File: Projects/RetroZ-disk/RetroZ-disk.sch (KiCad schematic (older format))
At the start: 22 parts, among them J1 Micro_SD_Card, J2 IO SELECTOR, Q1 2SA933, U1 UA78M33CDCYR, U2 74LS138, U3 TXB0104DW, U4 ATMEGA328P-PU, U5 74LS02, Y1 20Mhz

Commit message: added interrupt signal
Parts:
- added Q2: 2SA933, Package_TO_SOT_THT:TO-92S_Wide, symbol Device:Q_PNP_ECB
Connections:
- net GND: now also Q2.2 (C)
- net ~INT: now reaches I1.30 (~INT~)
- net ~INT: now also Q2.1 (E)
- net at U4.14 ((PCINT0/CLKO/ICP1)PB0): now also Q2.3 (B)
- no-connect marks 39 -> 37
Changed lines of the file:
@@
 NoConn ~ 1175 1400
 NoConn ~ 1175 1700
-NoConn ~ 1175 1800
 NoConn ~ 1175 2200
 NoConn ~ 1175 2400
@@
 Text Label 9900 5175 2    50   ~ 0
 ~WAIT
-NoConn ~ 7800 1550
 Text Label 8100 2800 2    50   ~ 0
 ~CS
@@
 	0    1    1    0
 $EndComp
+$Comp
+L Device:Q_PNP_ECB Q2
+U 1 1 5E6AC7AF
+P 8475 1200
+F 0 "Q2" H 8400 1075 50  0000 C CNN
+F 1 "2SA933" H 8800 1225 50  0000 C CNN
+F 2 "Package_TO_SOT_THT:TO-92S_Wide" H 8675 1300 50  0001 C CNN
+F 3 "https://media.digikey.com/pdf/Data%20Sheets/Micro%20Commercial%20PDFs/2SA933AS-x.pdf" H 8475 1200 50  0001 C CNN
+	1    8475 1200
+	1    0    0    1
+$EndComp
+$Comp
+L power:GND #PWR0101
+U 1 1 5E6C653E
+P 8575 1400
+F 0 "#PWR0101" H 8575 1150 50  0001 C CNN
+F 1 "GND" H 8575 1250 50  0000 C CNN
+F 2 "" H 8575 1400 50  0001 C CNN
+F 3 "" H 8575 1400 50  0001 C CNN
+	1    8575 1400
+	1    0    0    -1
+$EndComp
+Text Label 8750 1000 2    50   ~ 0
+~INT
+Wire Wire Line
+	8575 1000 8750 1000
+Wire Wire Line
+	7800 1550 7800 1200
+Wire Wire Line
+	7800 1200 8275 1200
+Text Label 925  1800 0    50   ~ 0
+~INT
+Wire Wire Line
+	1175 1800 925  1800
 Wire Bus Line
 	8075 3250 8075 4300

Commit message: fixed interrupt ack processing
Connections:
- net ~IORQ: now also U4.14 ((PCINT0/CLKO/ICP1)PB0)
- net ~M1: now reaches I1.31 (~M1~)
- net ~M1: now also U4.15 ((PCINT1/OC1A)PB1)
- net at Q2.3 (B): now also U4.28 ((PCINT13/SCL/ADC5)PC5); no longer U4.14 ((PCINT0/CLKO/ICP1)PB0)
- no-connect marks 37 -> 33
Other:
- moved on the sheet: Q2
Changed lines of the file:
@@
 Wire Wire Line
 	5400 5700 5400 5600
-NoConn ~ 1175 2100
 Text Notes 1900 5050 0    50   ~ 0
 5V to 3.3V,500mA
@@
 	0    -1   -1   0
 $EndComp
-NoConn ~ 5950 2575
 $Comp
 L power:VDD #PWR013
@@
 	1    0    0    -1
 $EndComp
-NoConn ~ 7800 1650
 Wire Wire Line
 	8700 1750 8925 1750
@@
 Wire Wire Line
 	9150 2800 9175 2800
-NoConn ~ 7800 2900
 $Comp
 L power:GND #PWR020
@@
 L Device:Q_PNP_ECB Q2
 U 1 1 5E6AC7AF
-P 8475 1200
-F 0 "Q2" H 8400 1075 50  0000 C CNN
-F 1 "2SA933" H 8800 1225 50  0000 C CNN
-F 2 "Package_TO_SOT_THT:TO-92S_Wide" H 8675 1300 50  0001 C CNN
-F 3 "https://media.digikey.com/pdf/Data%20Sheets/Micro%20Commercial%20PDFs/2SA933AS-x.pdf" H 8475 1200 50  0001 C CNN
-	1    8475 1200
+P 9025 2250
+F 0 "Q2" H 8950 2125 50  0000 C CNN
+F 1 "2SA933" H 9350 2275 50  0000 C CNN
+F 2 "Package_TO_SOT_THT:TO-92S_Wide" H 9225 2350 50  0001 C CNN
+F 3 "https://media.digikey.com/pdf/Data%20Sheets/Micro%20Commercial%20PDFs/2SA933AS-x.pdf" H 9025 2250 50  0001 C CNN
+	1    9025 2250
 	1    0    0    1
 $EndComp
@@
 L power:GND #PWR0101
 U 1 1 5E6C653E
-P 8575 1400
-F 0 "#PWR0101" H 8575 1150 50  0001 C CNN
-F 1 "GND" H 8575 1250 50  0000 C CNN
-F 2 "" H 8575 1400 50  0001 C CNN
-F 3 "" H 8575 1400 50  0001 C CNN
-	1    8575 1400
-	1    0    0    -1
-$EndComp
-Text Label 8750 1000 2    50   ~ 0
+P 9125 2450
+F 0 "#PWR0101" H 9125 2200 50  0001 C CNN
+F 1 "GND" H 9125 2300 50  0000 C CNN
+F 2 "" H 9125 2450 50  0001 C CNN
+F 3 "" H 9125 2450 50  0001 C CNN
+	1    9125 2450
+	1    0    0    -1
+$EndComp
+Text Label 9300 2050 2    50   ~ 0
 ~INT
 Wire Wire Line
-	8575 1000 8750 1000
-Wire Wire Line
-	7800 1550 7800 1200
-Wire Wire Line
-	7800 1200 8275 1200
+	9125 2050 9300 2050
 Text Label 925  1800 0    50   ~ 0
 ~INT
 Wire Wire Line
 	1175 1800 925  1800
+Wire Wire Line
+	1175 2100 925  2100
+Text Label 925  2100 0    50   ~ 0
+~M1
+Wire Wire Line
+	7800 1650 8100 1650
+Text Label 8100 1650 2    50   ~ 0
+~M1
+Text Label 8100 1550 2    50   ~ 0
+~IORQ
+Wire Wire Line
+	7800 1550 8100 1550
+Wire Wire Line
+	8825 2250 8800 2250
+Wire Wire Line
+	8800 2250 8800 2900
+Wire Wire Line
+	8800 2900 7800 2900
 Wire Bus Line
 	8075 3250 8075 4300

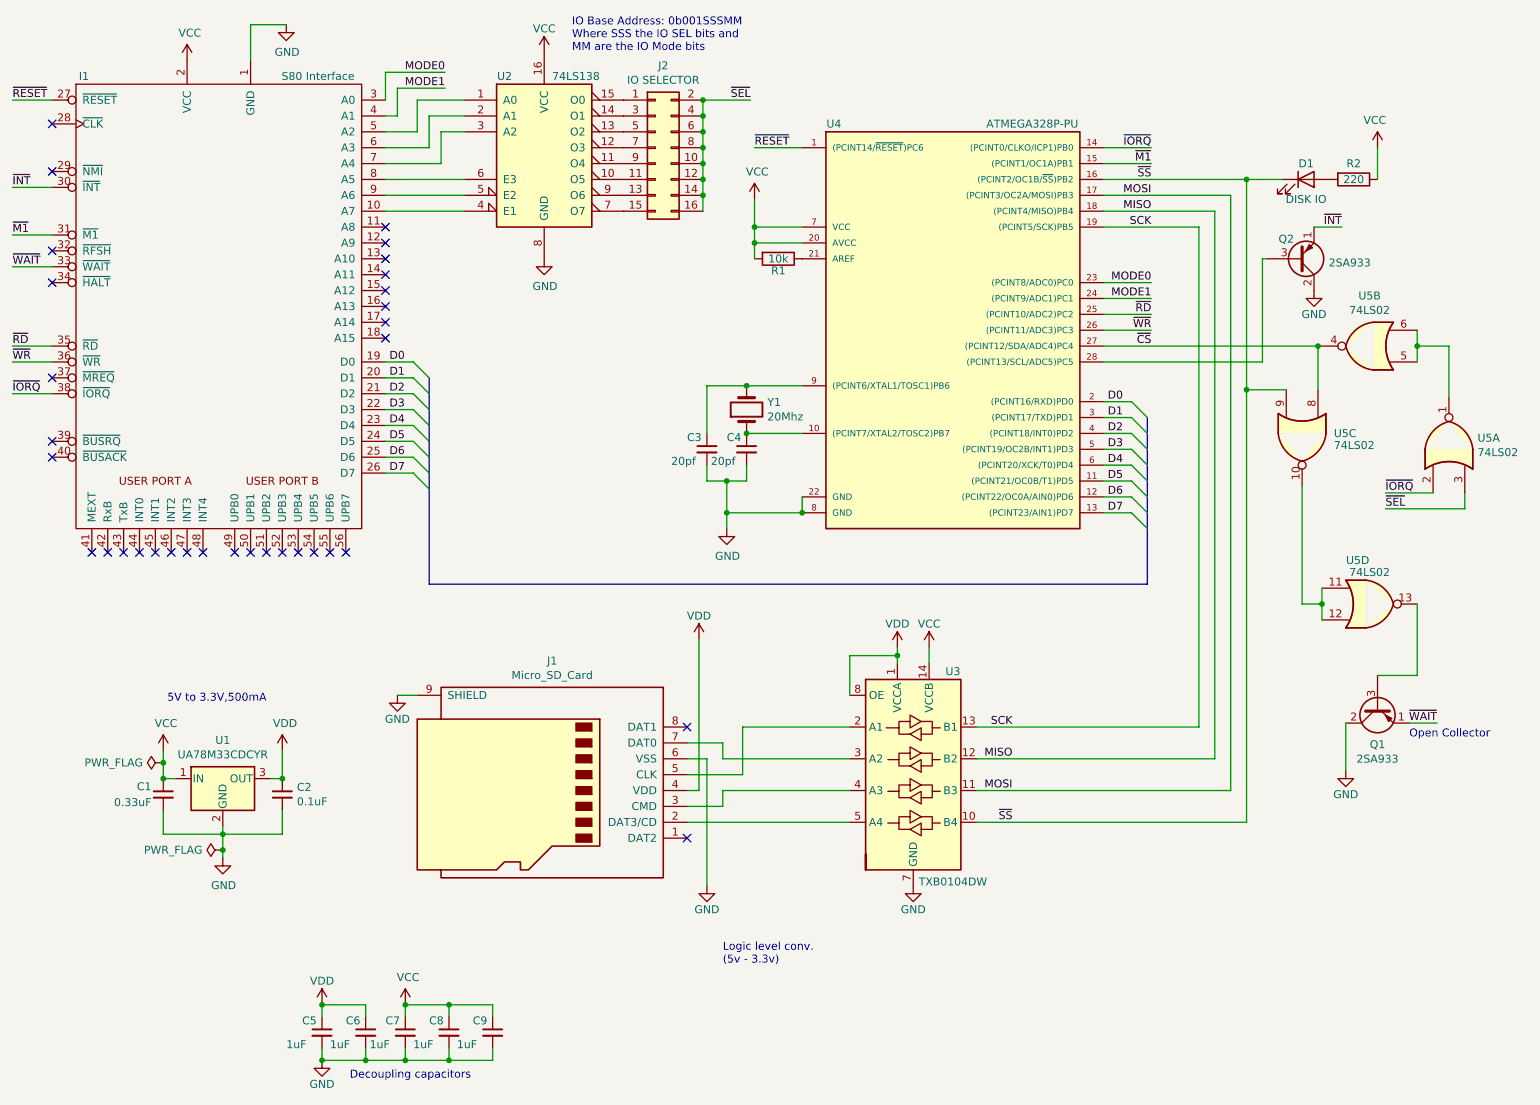
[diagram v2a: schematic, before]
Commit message: removed interrupt management, added arduino code
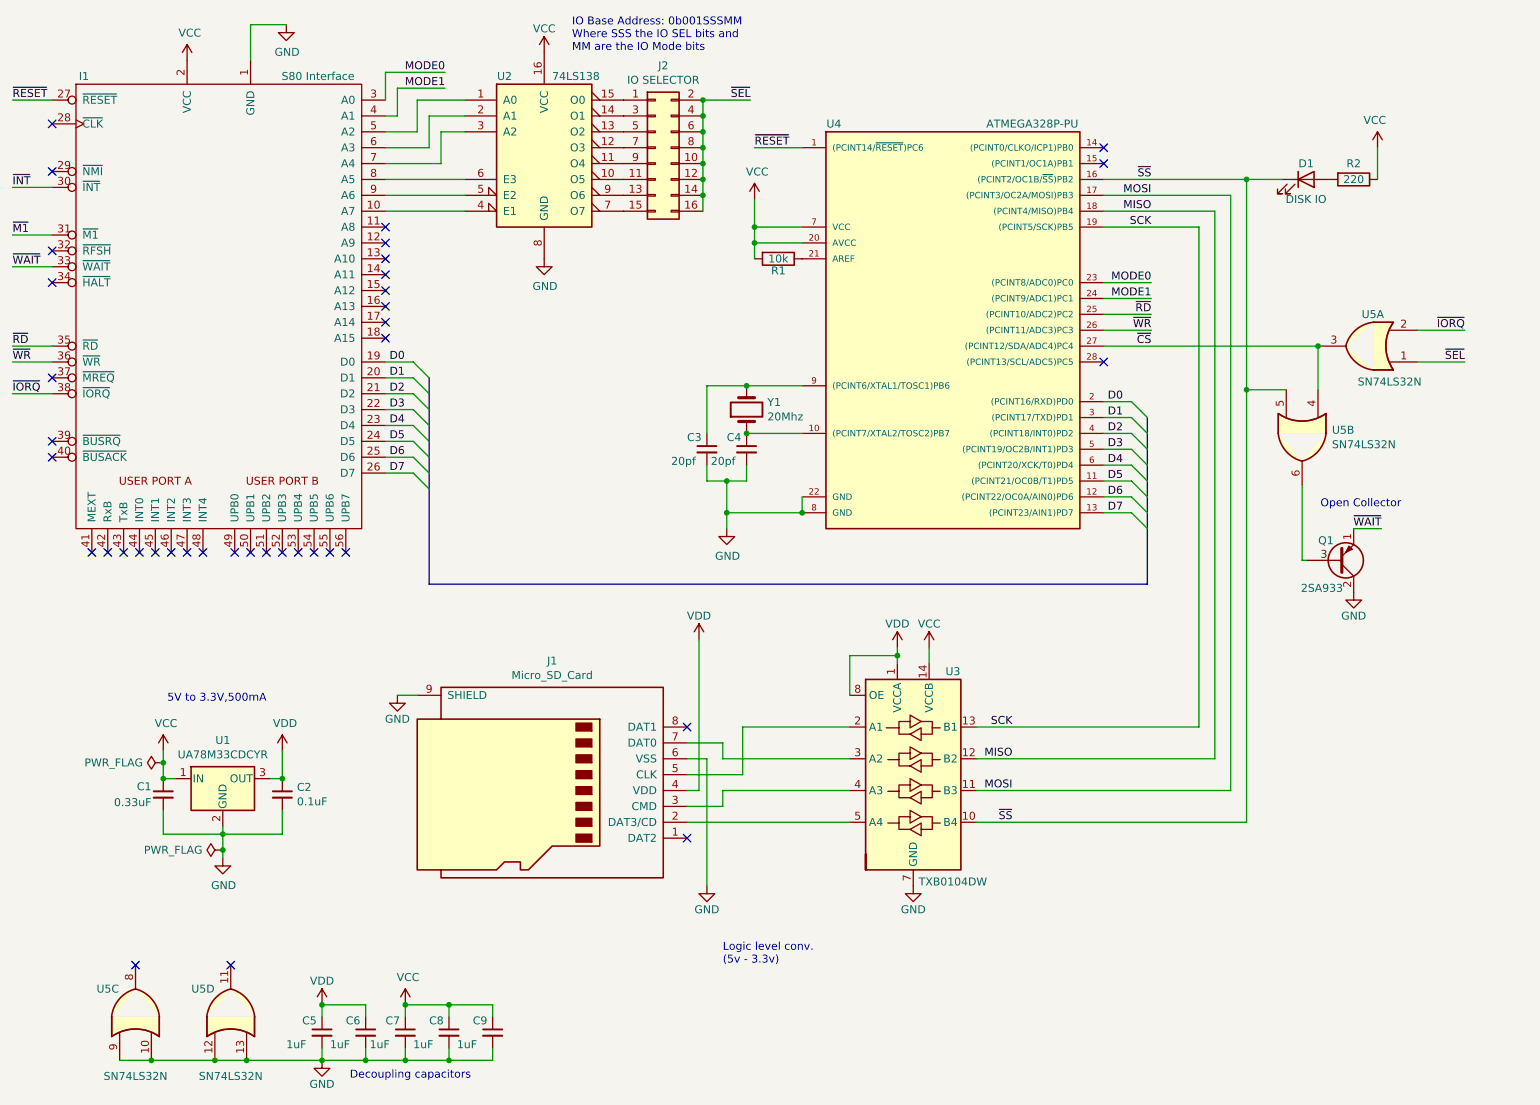
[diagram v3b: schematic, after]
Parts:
- removed Q2: 2SA933, Package_TO_SOT_THT:TO-92S_Wide, symbol Device:Q_PNP_ECB
- removed U5: 74LS02, symbol 74xx:7402
- added U5: SN74LS32N, Package_DIP:DIP-14_W7.62mm_LongPads, symbol 74xx:74LS32
- U2: footprint Housings_DIP:DIP-16_W7.62mm_Socket_LongPads -> Package_DIP:DIP-16_W7.62mm_LongPads
- U4: footprint Housings_DIP:DIP-28_W7.62mm_Socket_LongPads -> Package_DIP:DIP-28_W7.62mm_LongPads
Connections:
- net GND: now also U5.10, U5.12, U5.13, U5.9
- net ~CS: now also U5.3, U5.4
- net ~IORQ: now also U5.2; no longer U4.14 ((PCINT0/CLKO/ICP1)PB0)
- net ~M1: no longer U4.15 ((PCINT1/OC1A)PB1)
- net ~SEL: now also U5.1
- net ~SS: now also U5.5
- net at Q1.3 (B): now also U5.6
- no-connect marks 33 -> 38
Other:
- moved on the sheet: Q1
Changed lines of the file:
@@
 F 0 "U4" H 6100 3900 50  0000 C CNN
 F 1 "ATMEGA328P-PU" H 7350 3900 50  0000 C CNN
-F 2 "Housings_DIP:DIP-28_W7.62mm_Socket_LongPads" H 6800 2650 50  0001 C CIN
+F 2 "Package_DIP:DIP-28_W7.62mm_LongPads" H 6800 2650 50  0001 C CIN
 F 3 "https://www.mouser.ca/datasheet/2/268/Atmel-8271-8-bit-AVR-Microcontroller-ATmega48A-48P-1315288.pdf" H 6800 2650 50  0001 C CNN
 	1    6800 2650
@@
 F 0 "U2" H 4025 2000 50  0000 C CNN
 F 1 "74LS138" H 4475 2000 50  0000 C CNN
-F 2 "Housings_DIP:DIP-16_W7.62mm_Socket_LongPads" H 4275 1550 50  0001 C CNN
+F 2 "Package_DIP:DIP-16_W7.62mm_LongPads" H 4275 1550 50  0001 C CNN
 F 3 "http://www.ti.com/lit/gpn/sn74LS138" H 4275 1550 50  0001 C CNN
 F 4 "SN74HC138N" H 4275 1550 50  0001 C CNN "Mfr#"
@@
 Text Label 925  3100 0    50   ~ 0
 ~IORQ
-Text Label 9575 3725 0    50   ~ 0
+Text Label 10075 2700 2    50   ~ 0
 ~IORQ
 Wire Wire Line
-	9875 3725 9575 3725
+	9775 2700 10075 2700
 Text Label 5575 1250 2    50   ~ 0
 ~SEL
@@
 	5275 1250 5575 1250
 Connection ~ 5275 1250
-Text Label 9575 3825 0    50   ~ 0
+Text Label 10075 2900 2    50   ~ 0
 ~SEL
 Wire Bus Line
@@
 	2250 5875 2250 5975
 Connection ~ 2250 5975
-Text Label 9900 5175 2    50   ~ 0
+Text Label 9550 3950 2    50   ~ 0
 ~WAIT
 Text Label 8100 2800 2    50   ~ 0
 ~CS
-$Comp
-L 74xx:7402 U5
-U 2 1 5E2FF702
-P 9475 2800
-F 0 "U5" H 9475 2483 50  0000 C CNN
-F 1 "74LS02" H 9475 2574 50  0000 C CNN
-F 2 "" H 9475 2800 50  0001 C CNN
-F 3 "http://www.ti.com/lit/gpn/sn74ls02" H 9475 2800 50  0001 C CNN
-	2    9475 2800
-	-1   0    0    1
-$EndComp
-Wire Wire Line
-	9775 2700 9775 2800
-Wire Wire Line
-	9975 3125 9975 2800
-Wire Wire Line
-	9975 2800 9775 2800
-Connection ~ 9775 2800
-Wire Wire Line
-	9775 2800 9775 2900
-Wire Wire Line
-	10075 3825 10075 3725
-Wire Wire Line
-	9575 3825 10075 3825
 Wire Wire Line
 	3275 1750 3775 1750
 Text Notes 4450 950  0    50   ~ 0
 IO Base Address: 0b001SSSMM\nWhere SSS the IO SEL bits and\nMM are the IO Mode bits
-$Comp
-L 74xx:7402 U5
-U 1 1 5E34E3AC
-P 9975 3425
-F 0 "U5" V 10021 3245 50  0000 R CNN
-F 1 "74LS02" V 9930 3245 50  0000 R CNN
-F 2 "Housings_DIP:DIP-14_W7.62mm_Socket_LongPads" H 9975 3425 50  0001 C CNN
-F 3 "http://www.ti.com/lit/gpn/sn74ls02" H 9975 3425 50  0001 C CNN
-F 4 "SN74HC02NE4" V 9975 3425 50  0001 C CNN "Mfr#"
-	1    9975 3425
-	0    -1   -1   0
-$EndComp
 $Comp
 L power:VDD #PWR013
@@
 L power:GND #PWR020
 U 1 1 5E7A07A4
-P 9325 5475
-F 0 "#PWR020" H 9325 5225 50  0001 C CNN
-F 1 "GND" H 9325 5325 50  0000 C CNN
-F 2 "" H 9325 5475 50  0001 C CNN
-F 3 "" H 9325 5475 50  0001 C CNN
-	1    9325 5475
-	1    0    0    -1
-$EndComp
-Text Notes 9725 5275 0    50   ~ 0
+P 9375 4350
+F 0 "#PWR020" H 9375 4100 50  0001 C CNN
+F 1 "GND" H 9375 4200 50  0000 C CNN
+F 2 "" H 9375 4350 50  0001 C CNN
+F 3 "" H 9375 4350 50  0001 C CNN
+	1    9375 4350
+	1    0    0    -1
+$EndComp
+Text Notes 9675 3825 2    50   ~ 0
 Open Collector
 Wire Wire Line
-	9725 5175 9900 5175
+	9375 3950 9550 3950
 $Comp
 L Device:Q_PNP_ECB Q1
 U 1 1 5E7F9FF3
-P 9525 5075
-F 0 "Q1" V 9760 5075 50  0000 C CNN
-F 1 "2SA933" V 9851 5075 50  0000 C CNN
-F 2 "Package_TO_SOT_THT:TO-92S_Wide" H 9725 5175 50  0001 C CNN
-F 3 "https://media.digikey.com/pdf/Data%20Sheets/Micro%20Commercial%20PDFs/2SA933AS-x.pdf" H 9525 5075 50  0001 C CNN
-	1    9525 5075
-	0    -1   1    0
-$EndComp
-Wire Wire Line
-	9325 5175 9325 5475
-Wire Wire Line
-	9175 4325 9175 4425
-Wire Wire Line
-	9050 3675 9050 4425
-Wire Wire Line
-	9050 4425 9175 4425
-Connection ~ 9175 4425
-Wire Wire Line
-	9175 4425 9175 4525
-Wire Wire Line
-	9775 4425 9775 4875
-Wire Wire Line
-	9775 4875 9525 4875
-$Comp
-L 74xx:7402 U5
-U 4 1 5E88BC6D
-P 9475 4425
-F 0 "U5" H 9400 4700 50  0000 C CNN
-F 1 "74LS02" H 9475 4625 50  0000 C CNN
-F 2 "" H 9475 4425 50  0001 C CNN
-F 3 "http://www.ti.com/lit/gpn/sn74ls02" H 9475 4425 50  0001 C CNN
-	4    9475 4425
-	1    0    0    -1
-$EndComp
-$Comp
-L 74xx:7402 U5
-U 3 1 5E8A09DC
-P 9050 3375
-F 0 "U5" V 9025 3575 50  0000 L CNN
-F 1 "74LS02" V 9100 3575 50  0000 L CNN
-F 2 "" H 9050 3375 50  0001 C CNN
-F 3 "http://www.ti.com/lit/gpn/sn74ls02" H 9050 3375 50  0001 C CNN
-F 4 "SN74HC02NE4" V 9050 3375 50  0001 C CNN "Mfr#"
-	3    9050 3375
-	0    1    1    0
-$EndComp
-$Comp
-L Device:Q_PNP_ECB Q2
-U 1 1 5E6AC7AF
-P 9025 2250
-F 0 "Q2" H 8950 2125 50  0000 C CNN
-F 1 "2SA933" H 9350 2275 50  0000 C CNN
-F 2 "Package_TO_SOT_THT:TO-92S_Wide" H 9225 2350 50  0001 C CNN
-F 3 "https://media.digikey.com/pdf/Data%20Sheets/Micro%20Commercial%20PDFs/2SA933AS-x.pdf" H 9025 2250 50  0001 C CNN
-	1    9025 2250
+P 9275 4150
+F 0 "Q1" H 9200 4025 50  0000 C CNN
+F 1 "2SA933" H 9175 4325 50  0000 C CNN
+F 2 "Package_TO_SOT_THT:TO-92S_Wide" H 9475 4250 50  0001 C CNN
+F 3 "https://media.digikey.com/pdf/Data%20Sheets/Micro%20Commercial%20PDFs/2SA933AS-x.pdf" H 9275 4150 50  0001 C CNN
+	1    9275 4150
 	1    0    0    1
 $EndComp
-$Comp
-L power:GND #PWR0101
-U 1 1 5E6C653E
-P 9125 2450
-F 0 "#PWR0101" H 9125 2200 50  0001 C CNN
-F 1 "GND" H 9125 2300 50  0000 C CNN
-F 2 "" H 9125 2450 50  0001 C CNN
-F 3 "" H 9125 2450 50  0001 C CNN
-	1    9125 2450
-	1    0    0    -1
-$EndComp
-Text Label 9300 2050 2    50   ~ 0
-~INT
-Wire Wire Line
-	9125 2050 9300 2050
 Text Label 925  1800 0    50   ~ 0
 ~INT
@@
 Text Label 925  2100 0    50   ~ 0
 ~M1
-Wire Wire Line
-	7800 1650 8100 1650
-Text Label 8100 1650 2    50   ~ 0
-~M1
-Text Label 8100 1550 2    50   ~ 0
-~IORQ
-Wire Wire Line
-	7800 1550 8100 1550
-Wire Wire Line
-	8825 2250 8800 2250
-Wire Wire Line
-	8800 2250 8800 2900
-Wire Wire Line
-	8800 2900 7800 2900
+$Comp
+L 74xx:74LS32 U5
+U 1 1 5E7FD5C4
+P 9475 2800
+F 0 "U5" H 9525 2600 50  0000 R CNN
+F 1 "SN74LS32N" H 9550 3025 50  0000 R CNN
+F 2 "Package_DIP:DIP-14_W7.62mm_LongPads" H 9475 2800 50  0001 C CNN
+F 3 "http://www.ti.com/lit/gpn/sn74LS32" H 9475 2800 50  0001 C CNN
+	1    9475 2800
+	-1   0    0    1
+$EndComp
+Wire Wire Line
+	9775 2900 10075 2900
+$Comp
+L 74xx:74LS32 U5
+U 2 1 5E83A9D0
+P 9050 3375
+F 0 "U5" V 9004 3563 50  0000 L CNN
+F 1 "SN74LS32N" V 9095 3563 50  0000 L CNN
+F 2 "Package_DIP:DIP-14_W7.62mm_LongPads" H 9050 3375 50  0001 C CNN
+F 3 "http://www.ti.com/lit/gpn/sn74LS32" H 9050 3375 50  0001 C CNN
+	2    9050 3375
+	0    1    1    0
+$EndComp
+Wire Wire Line
+	9050 3675 9050 4150
+Wire Wire Line
+	9050 4150 9075 4150
+$Comp
+L 74xx:74LS32 U5
+U 3 1 5E886F65
+P 1700 7000
+F 0 "U5" V 1850 7175 50  0000 C CNN
+F 1 "SN74LS32N" V 1300 7000 50  0000 C CNN
+F 2 "Package_DIP:DIP-14_W7.62mm_LongPads" H 1700 7000 50  0001 C CNN
+F 3 "http://www.ti.com/lit/gpn/sn74LS32" H 1700 7000 50  0001 C CNN
+	3    1700 7000
+	0    -1   -1   0
+$EndComp
+$Comp
+L 74xx:74LS32 U5
+U 4 1 5E8895AC
+P 2300 7000
+F 0 "U5" V 2450 7175 50  0000 C CNN
+F 1 "SN74LS32N" V 1900 7000 50  0000 C CNN
+F 2 "Package_DIP:DIP-14_W7.62mm_LongPads" H 2300 7000 50  0001 C CNN
+F 3 "http://www.ti.com/lit/gpn/sn74LS32" H 2300 7000 50  0001 C CNN
+	4    2300 7000
+	0    -1   -1   0
+$EndComp
+NoConn ~ 1700 6700
+NoConn ~ 2300 6700
+Wire Wire Line
+	2875 7300 2400 7300
+Connection ~ 1800 7300
+Wire Wire Line
+	1800 7300 1600 7300
+Connection ~ 2200 7300
+Wire Wire Line
+	2200 7300 1800 7300
+Connection ~ 2400 7300
+Wire Wire Line
+	2400 7300 2200 7300
+NoConn ~ 7800 2900
+NoConn ~ 7800 1550
+NoConn ~ 7800 1650
 Wire Bus Line
 	8075 3250 8075 4300
